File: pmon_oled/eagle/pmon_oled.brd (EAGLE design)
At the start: 60 x 60 mm, 37 parts, among them J1 USB, J2 USB, J4 PINHD-1X3, J5 PINHD-2X3, Q1 16Mhz, U1 LTC2943, U2 FT232RL, U3 LT1764AEQ, U4 ATMEGA328TQFP32

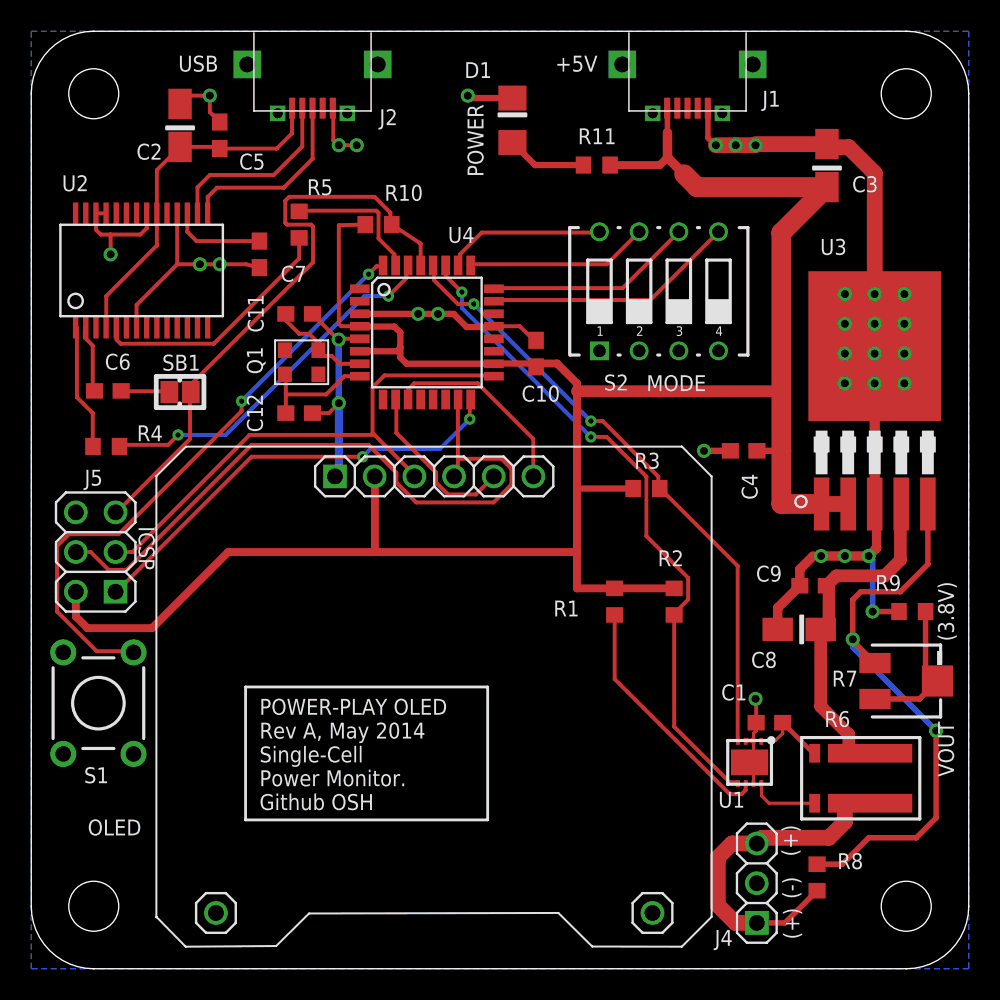
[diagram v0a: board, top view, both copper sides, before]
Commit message: Removed the config dip switches.
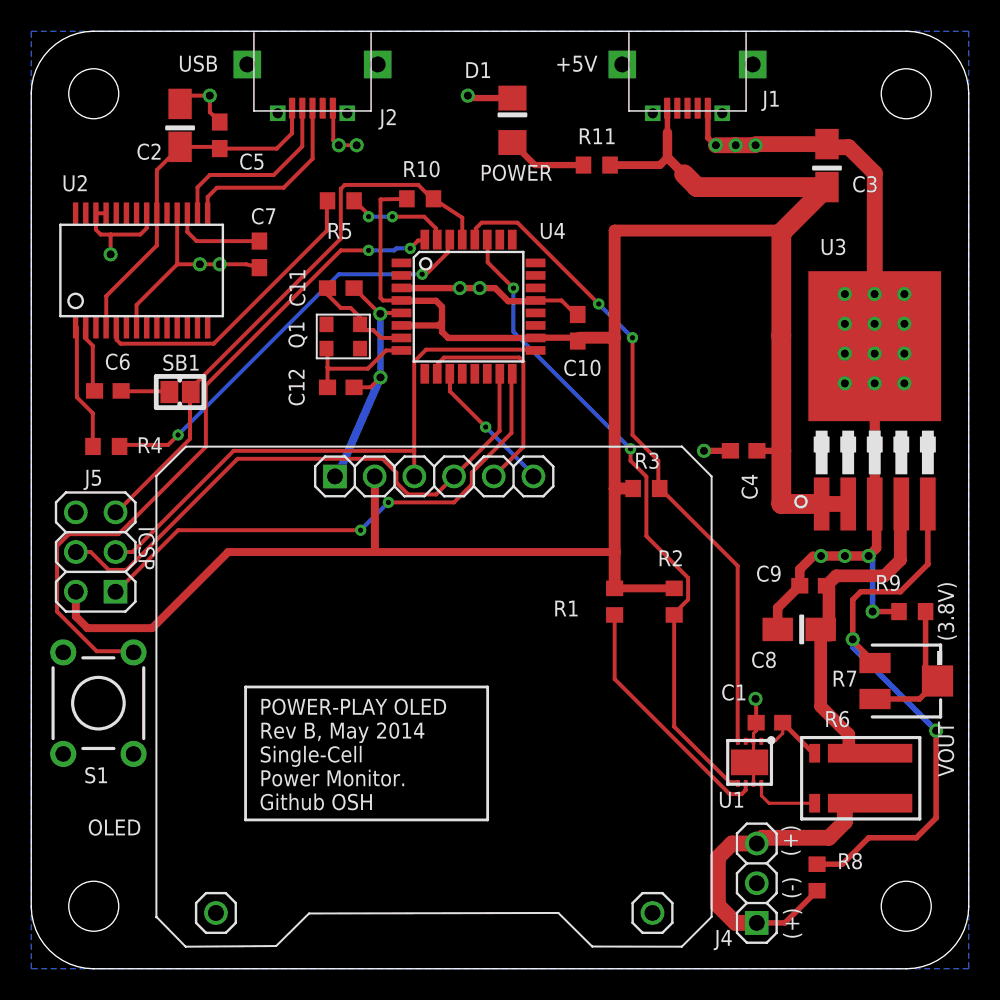
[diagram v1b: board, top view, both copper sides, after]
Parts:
- removed S2: DIP_SWITCH-X4, pmon_oled:DIP-SWITCH-X4
- moved C10 3.14 mm to (35.0, 41.0)
- moved C11 3.14 mm to (19.8, 43.6)
- moved Q1 3.14 mm to (20.0, 40.5)
- moved R10 3.14 mm to (24.9, 49.3)
- moved U4 3.14 mm to (28.0, 42.4)
- moved C12 3.14 mm to (19.8, 37.2)
- moved R5 3.07 mm to (19.8, 49.1), turned to 180 degrees
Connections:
- removed net CONFIG1: S2.8, U4.26
- removed net CONFIG2: S2.7, U4.25
- removed net CONFIG3: S2.6, U4.24
- removed net CONFIG4: S2.5, U4.23
- net GND: no longer S2.1, S2.2, S2.3, S2.4
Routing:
- net CONFIG4: track 16.2 -> 0.00 mm
- net CONFIG3: track 13.3 -> 0.00 mm
- net CONFIG2: track 11.7 -> 0.00 mm
- net CONFIG1: track 10.3 -> 0.00 mm
- net MOSI: track 43.8 -> 37.2 mm
- net START: track 38.9 -> 44.1 mm
- net MISO: track 28.5 -> 33.8 mm
- net +5V: track 155.1 -> 159.4 mm
- net OLED_D/C: track 12.7 -> 8.78 mm, vias 0 -> 1
- net OLED_RST: track 10.9 -> 14.6 mm
- net SER_RX: track 23.7 -> 27.1 mm
- net N$8: track 16.1 -> 19.3 mm
- net I2C-CLK: track 39.6 -> 42.7 mm
- net SCK: track 34.7 -> 37.4 mm
- net GND: track 121.1 -> 123.4 mm
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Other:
- board text added: "POWER-PLAY OLED - REV B OSH GITHUB"
- board text added: "POWER-PLAY OLED Rev B, May 2014 Single-Cell Power Monitor. Github OSH"
- board text removed: "MODE"
- board text removed: "POWER-PLAY OLED - REV A OSH GITHUB"
- board text removed: "POWER-PLAY OLED Rev A, May 2014 Single-Cell Power Monitor. Github OSH"

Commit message: Updated library (larger header pads) and auto rerouted.
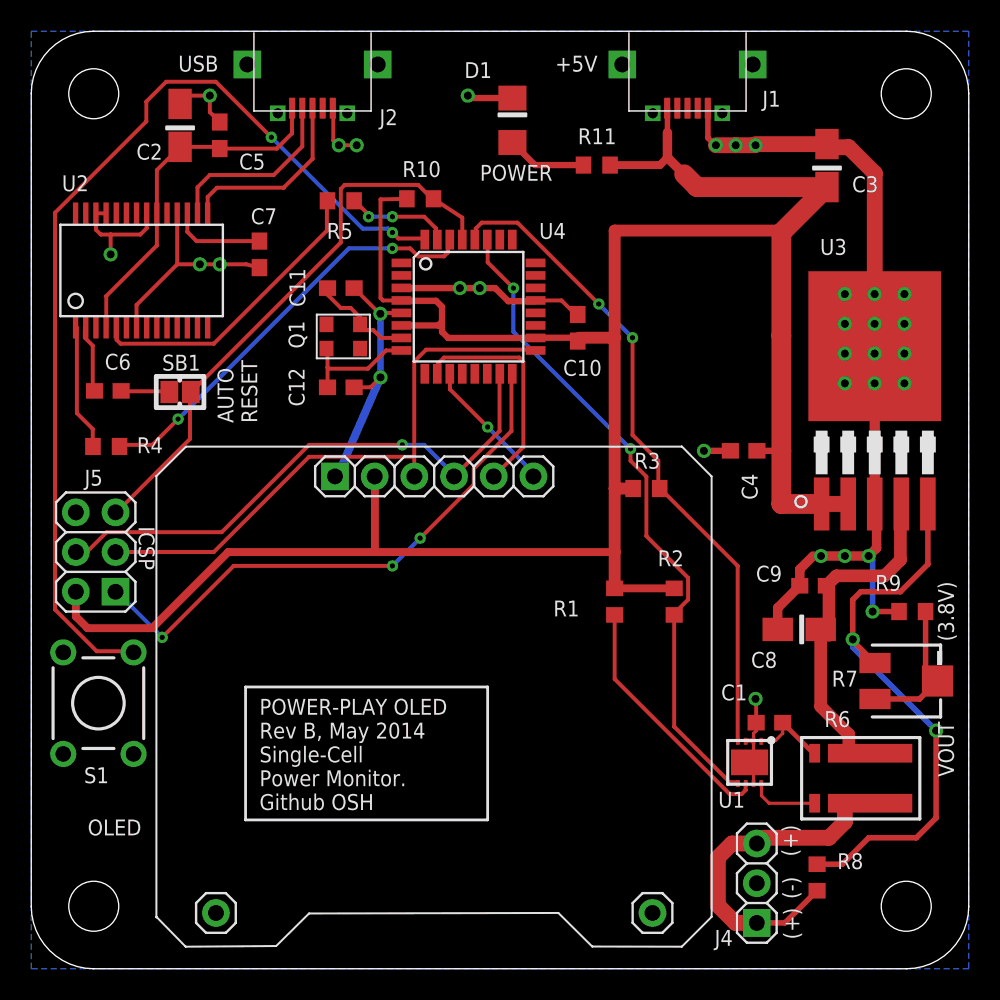
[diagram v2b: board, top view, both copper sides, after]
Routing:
- net START: track 44.1 -> 63.6 mm
- net MISO: track 33.8 -> 36.3 mm, vias 2 -> 3
- net MOSI: track 37.2 -> 35.7 mm, vias 0 -> 1
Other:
- board text added: "AUTO RESET"
